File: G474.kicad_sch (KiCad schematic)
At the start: 25 parts, among them J1 Conn_ST_STDC14, J30 Conn_01x04_Pin, SW1 SW_Push, SW2 SW_Push, SW3 SW_Push, U1 STM32G474RETx, Y1 TSX-3225 24.0000MF20G-AC3

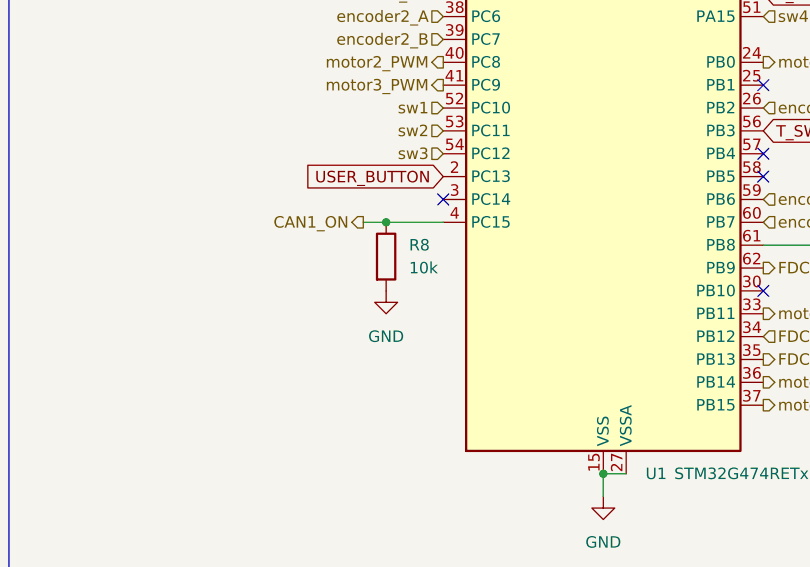
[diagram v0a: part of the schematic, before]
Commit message: 余計な抵抗を削除
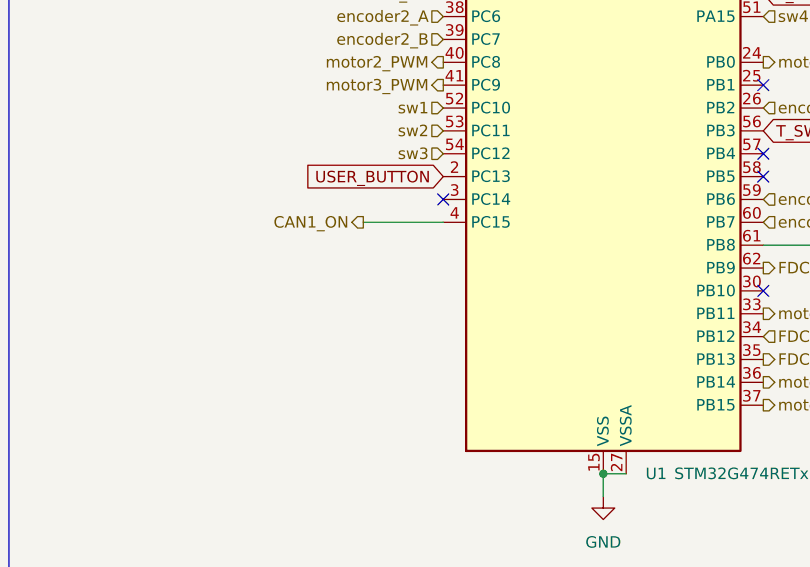
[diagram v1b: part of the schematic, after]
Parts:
- removed R8: 10k, Resistor_SMD:R_0603_1608Metric_Pad0.98x0.95mm_HandSolder, symbol Device:R
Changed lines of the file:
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@@
 	)
 	(junction
-		(at 179.07 115.57)
-		(diameter 0)
-		(color 0 0 0 0)
-	)
-	(junction
 		(at 257.81 29.21)
 		(diameter 0)
@@
 	(wire
 		(pts
-			(xy 176.53 115.57) (xy 179.07 115.57)
+			(xy 176.53 115.57) (xy 185.42 115.57)
 		)
 		(stroke
@@
 	(wire
 		(pts
-			(xy 179.07 115.57) (xy 185.42 115.57)
-		)
-		(stroke
-			(width 0)
-			(type default)
-		)
-	)
-	(wire
-		(pts
 			(xy 245.11 36.83) (xy 257.81 36.83)
 		)
@@
 	)
 	(symbol
-		(lib_id "Device:R")
-		(at 179.07 119.38 0)
-		(unit 1)
-		(body_style 1)
-		(exclude_from_sim no)
-		(in_bom yes)
-		(on_board yes)
-		(in_pos_files yes)
-		(dnp no)
-		(fields_autoplaced yes)
-		(property "Reference" "R8"
-			(at 181.61 118.1099 0)
-			(show_name no)
-			(do_not_autoplace no)
-			(effects
-				(font
-					(size 1.27 1.27)
-				)
-				(justify left)
-			)
-		)
-		(property "Value" "10k"
-			(at 181.61 120.6499 0)
-			(show_name no)
-			(do_not_autoplace no)
-			(effects
-				(font
-					(size 1.27 1.27)
-				)
-				(justify left)
-			)
-		)
-		(property "Footprint" "Resistor_SMD:R_0603_1608Metric_Pad0.98x0.95mm_HandSolder"
-			(at 177.292 119.38 90)
-			(hide yes)
-			(show_name no)
-			(do_not_autoplace no)
-			(effects
-				(font
-					(size 1.27 1.27)
-				)
-			)
-		)
-		(property "Datasheet" ""
-			(at 179.07 119.38 0)
-			(hide yes)
-			(show_name no)
-			(do_not_autoplace no)
-			(effects
-				(font
-					(size 1.27 1.27)
-				)
-			)
-		)
-		(property "Description" "Resistor"
-			(at 179.07 119.38 0)
-			(hide yes)
-			(show_name no)
-			(do_not_autoplace no)
-			(effects
-				(font
-					(size 1.27 1.27)
-				)
-			)
-		)
-		(property "KLC_S3.3" ""
-			(at 179.07 119.38 0)
-			(hide yes)
-			(show_name no)
-			(do_not_autoplace no)
-			(effects
-				(font
-					(size 1.27 1.27)
-				)
-			)
-		)
-		(property "KLC_S4.1" ""
-			(at 179.07 119.38 0)
-			(hide yes)
-			(show_name no)
-			(do_not_autoplace no)
-			(effects
-				(font
-					(size 1.27 1.27)
-				)
-			)
-		)
-		(property "LCSC" " C25804"
-			(at 179.07 119.38 0)
-			(hide yes)
-			(show_name no)
-			(do_not_autoplace no)
-			(effects
-				(font
-					(size 1.27 1.27)
-				)
-			)
-		)
-		(pin "1"
-		)
-		(pin "2"
-		)
-		(instances
-			(project "G474re_testboard_v2"
-				(path "/6701889f-a5e5-428d-8ee0-a9bdb287356c/6eeac764-06a5-469f-a340-9ffecc363115"
-					(reference "R8")
-					(unit 1)
-				)
-			)
-		)
-	)
-	(symbol
 		(lib_id "Device:C")
 		(at 44.45 80.01 0)
@@
 					(unit 1)
 				)
-			)
-		)
-	)
-	(symbol
-		(lib_id "power:GND")
-		(at 179.07 123.19 0)
-		(unit 1)
-		(body_style 1)
-		(exclude_from_sim no)
-		(in_bom yes)
-		(on_board yes)
-		(in_pos_files yes)
-		(dnp no)
-		(fields_autoplaced yes)
-		(property "Reference" "#PWR087"
-			(at 179.07 129.54 0)
-			(hide yes)
-			(show_name no)
-			(do_not_autoplace no)
-			(effects
-				(font
-					(size 1.27 1.27)
-				)
-			)
-		)
-		(property "Value" "GND"
-			(at 179.07 128.27 0)
-			(show_name no)
-			(do_not_autoplace no)
-			(effects
-				(font
-					(size 1.27 1.27)
-				)
-			)
-		)
-		(property "Footprint" ""
-			(at 179.07 123.19 0)
-			(hide yes)
-			(show_name no)
-			(do_not_autoplace no)
-			(effects
-				(font
-					(size 1.27 1.27)
-				)
-			)
-		)
-		(property "Datasheet" ""
-			(at 179.07 123.19 0)
-			(hide yes)
-			(show_name no)
-			(do_not_autoplace no)
-			(effects
-				(font
-					(size 1.27 1.27)
-				)
-			)
-		)
-		(property "Description" "Power symbol creates a global label with name \"GND\" , ground"
-			(at 179.07 123.19 0)
-			(hide yes)
-			(show_name no)
-			(do_not_autoplace no)
-			(effects
-				(font
-					(size 1.27 1.27)
-				)
-			)
-		)
-		(pin "1"
-		)
-		(instances
-			(project "G474re_testboard_v2"
-				(path "/6701889f-a5e5-428d-8ee0-a9bdb287356c/6eeac764-06a5-469f-a340-9ffecc363115"
-					(reference "#PWR087")
-					(unit 1)
-				)
